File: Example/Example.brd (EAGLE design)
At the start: 86 x 54 mm, 25 parts, among them IC2 74LS02D, U1 CD4017

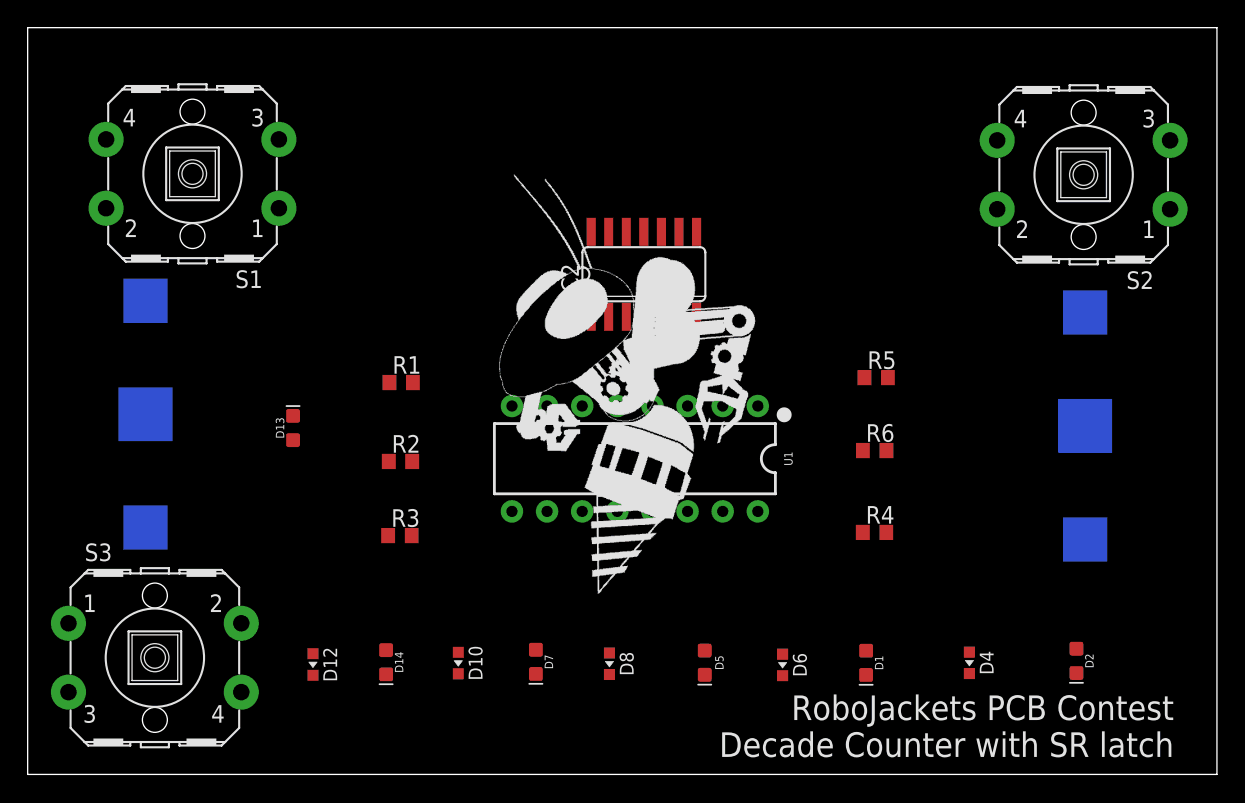
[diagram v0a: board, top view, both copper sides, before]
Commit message: made few routes except for gnd and vcc
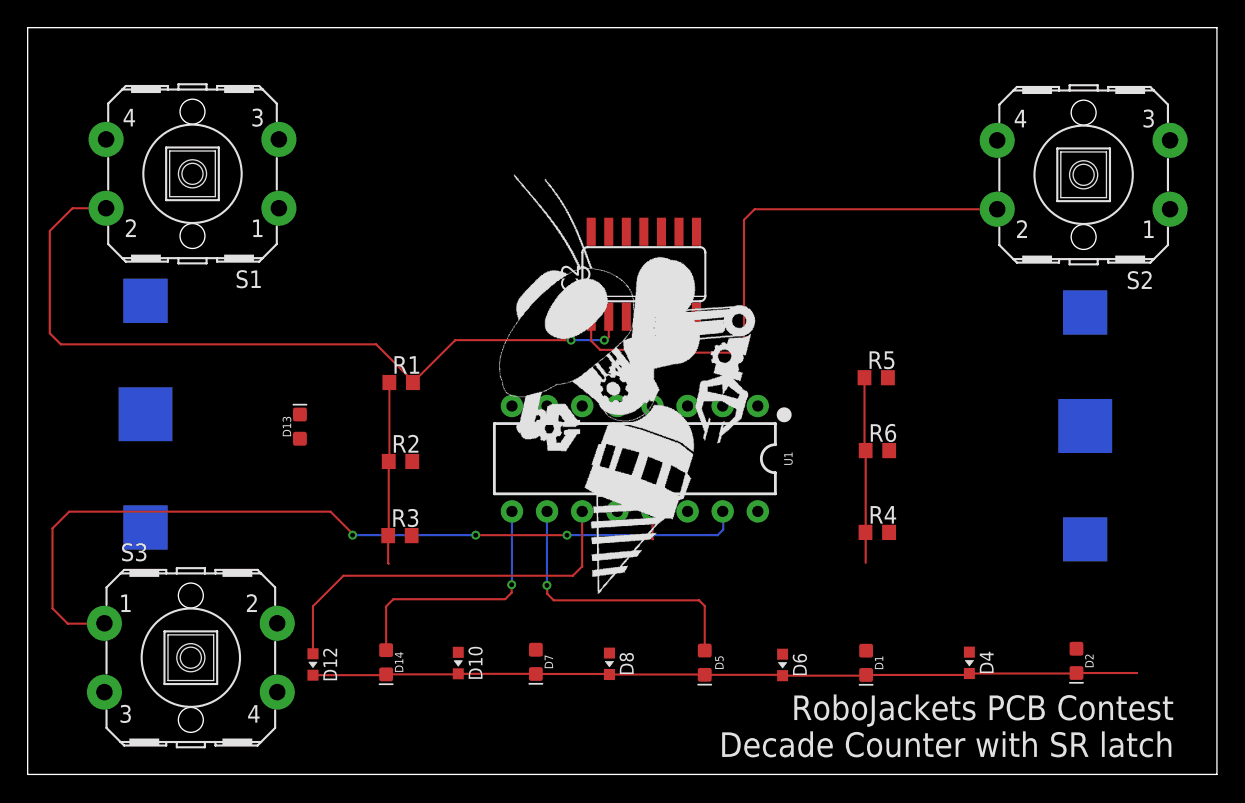
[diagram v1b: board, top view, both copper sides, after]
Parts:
- moved S3 2.60 mm to (11.8, 8.44)
- moved D13 0.51 mm to (19.7, 25.1)
- moved R6 0.20 mm to (61.5, 23.4)
- moved R4 0.20 mm to (61.4, 17.5)
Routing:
- net N$3: track 0.00 -> 61.3 mm, vias 0 -> 3
- net N$20: track 0.00 -> 59.7 mm
- net R: track 0.00 -> 56.9 mm, vias 0 -> 2
- net S: track 0.00 -> 34.6 mm
- net GND: track 0.00 -> 30.4 mm
- net N$19: track 0.00 -> 28.1 mm
- net N$14: track 0.00 -> 21.0 mm, vias 0 -> 1
- net N$18: track 0.00 -> 18.6 mm, vias 0 -> 1
- net Q: track 0.00 -> 9.06 mm

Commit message: add vcc and gnd planes and finished routing
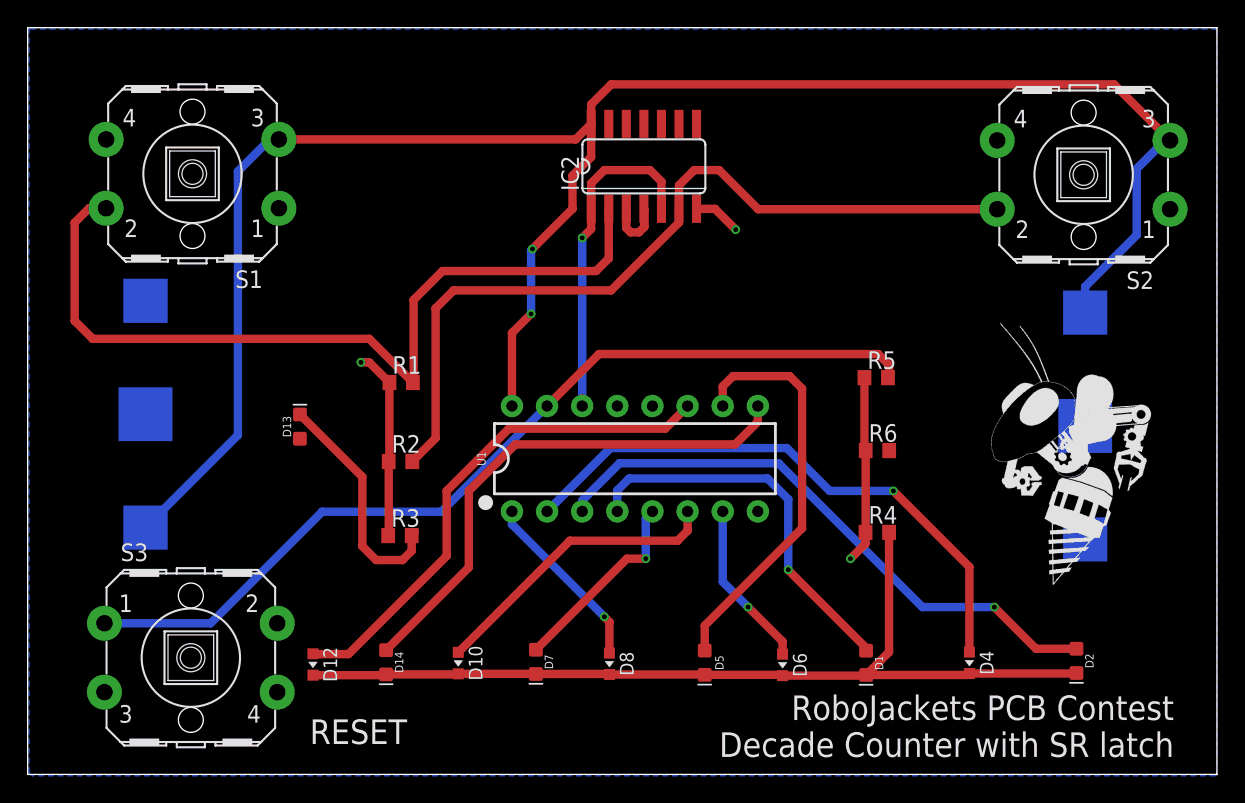
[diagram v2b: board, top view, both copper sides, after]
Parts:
- removed U$2: (no value), RoboJackets-Aesthetics:ROBOBUZZ_1.4X
- added U$4: (no value), RoboJackets-Aesthetics:ROBOBUZZ_1.0X
- moved IC2 7.80 mm to (44.6, 44.0)
- turned U1 to 0 degrees
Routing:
- net VCC: track 0.00 -> 139.0 mm, vias 0 -> 2
- net N$10: track 0.00 -> 43.2 mm, vias 0 -> 1
- net N$11: track 0.00 -> 42.2 mm, vias 0 -> 1
- net N$12: track 0.00 -> 28.1 mm, vias 0 -> 1
- net S: track 34.6 -> 59.3 mm
- net N$17: track 0.00 -> 21.7 mm
- net N$18: track 18.6 -> 38.1 mm, vias 1 -> 0
- net N$5: track 0.00 -> 17.1 mm
- net Q: track 9.06 -> 24.7 mm, vias 0 -> 1
- net N$16: track 0.00 -> 14.3 mm, vias 0 -> 1
- net N$15: track 0.00 -> 13.2 mm, vias 0 -> 1
- net N$13: track 0.00 -> 12.1 mm, vias 0 -> 1
- net N$19: track 28.1 -> 37.3 mm
- net N$14: track 21.0 -> 29.7 mm, vias 1 -> 0
- net N$20: track 59.7 -> 66.4 mm
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- added copper zone on layer 16, net GND
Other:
- board text added: "RESET"

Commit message: Added a layer for Vcc and GND, removed some routes
The GND routes and Vcc routes are connected to vias
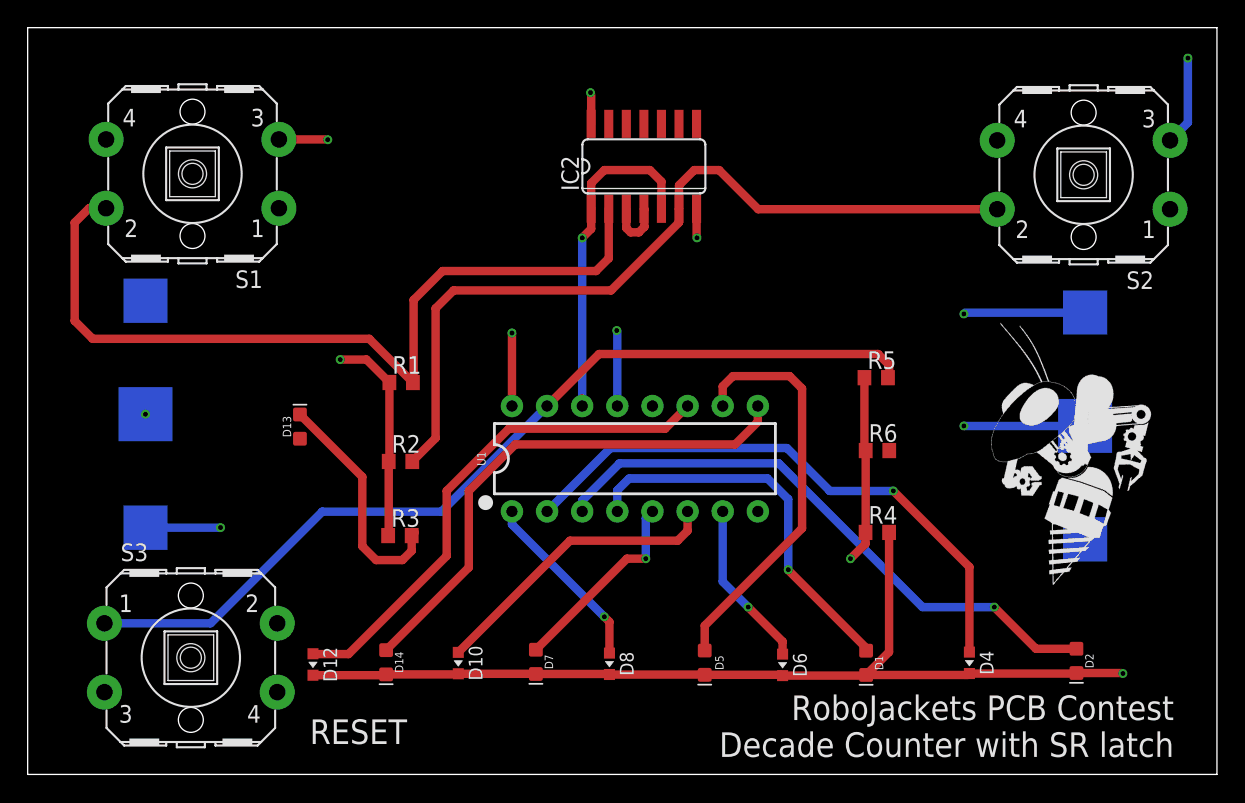
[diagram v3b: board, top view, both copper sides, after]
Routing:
- net VCC: track 139.0 -> 31.9 mm, vias 2 -> 6
- net GND: track 30.9 -> 45.6 mm, vias 3 -> 6
- net N$20: track 66.4 -> 69.8 mm, vias 0 -> 1
- removed copper zone on layer 16, net GND

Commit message: small changes
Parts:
- moved D13 1.28 mm to (20.7, 25.9)
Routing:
- net Q: track 24.7 -> 59.1 mm, vias 1 -> 3
- net VCC: track 31.9 -> 13.8 mm, vias 6 -> 3
- net GND: track 45.6 -> 29.0 mm, vias 6 -> 2
- net N$20: track 69.8 -> 66.4 mm, vias 1 -> 0
- net N$5: track 17.1 -> 18.7 mm
- net S: track 59.3 -> 60.6 mm
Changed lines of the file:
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@@
 <?xml version="1.0" encoding="utf-8"?>
 <!DOCTYPE eagle SYSTEM "eagle.dtd">
-<eagle version="9.5.2">
+<eagle version="9.5.1">
 <drawing>
 <settings>
-<setting alwaysvectorfont="no"/>
+<setting alwaysvectorfont="yes"/>
 <setting verticaltext="up"/>
 </settings>
@@
 <attribute name="VALUE" x="75.205" y="8.21" size="0.6096" layer="27" font="vector" ratio="20" rot="R270" align="top-center"/>
 </element>
-<element name="D13" library="RoboJackets-LEDs" package="LED-0603" value="GREEN" x="19.69" y="25.15" smashed="yes" rot="R90">
-<attribute name="NAME" x="19.055" y="25.15" size="0.6096" layer="25" font="vector" ratio="20" rot="R90" align="bottom-center"/>
-<attribute name="PROD_ID" value="DIO-00821" x="19.69" y="25.15" size="1.778" layer="27" rot="R90" display="off"/>
-<attribute name="VALUE" x="20.325" y="25.15" size="0.6096" layer="27" font="vector" ratio="20" rot="R90" align="top-center"/>
+<element name="D13" library="RoboJackets-LEDs" package="LED-0603" value="GREEN" x="20.69" y="25.95" smashed="yes" rot="R90">
+<attribute name="NAME" x="20.055" y="25.95" size="0.6096" layer="25" font="vector" ratio="20" rot="R90" align="bottom-center"/>
+<attribute name="PROD_ID" value="DIO-00821" x="20.69" y="25.95" size="1.778" layer="27" rot="R90" display="off"/>
+<attribute name="VALUE" x="21.325" y="25.95" size="0.6096" layer="27" font="vector" ratio="20" rot="R90" align="top-center"/>
 </element>
 <element name="D14" library="RoboJackets-LEDs" package="LED-0603" value="BLUE" x="25.92" y="8.11" smashed="yes" rot="R270">
@@
 <signals>
 <signal name="GND">
-<contactref element="IC2" pad="7"/>
 <contactref element="R1" pad="1"/>
 <contactref element="R2" pad="1"/>
@@
 <wire x1="26.11" y1="22.63" x2="26.11" y2="17.31" width="0.6096" layer="1"/>
 <wire x1="26.11" y1="17.31" x2="26.07" y2="17.27" width="0.1524" layer="1"/>
-<wire x1="48.4" y1="40.8666" x2="48.37" y2="40.8966" width="0.1524" layer="1"/>
 <wire x1="60.51" y1="28.69" x2="60.51" y2="23.51" width="0.6096" layer="1"/>
 <wire x1="60.51" y1="23.51" x2="60.6" y2="23.42" width="0.1524" layer="1"/>
@@
 <wire x1="24.5" y1="30" x2="22.6" y2="30" width="0.6096" layer="1"/>
 <via x="22.6" y="30" extent="1-16" drill="0.35"/>
-<via x="8.52" y="26.05" extent="1-16" drill="0.35"/>
-<wire x1="48.2" y1="40.7266" x2="48.37" y2="40.8966" width="0.1524" layer="1"/>
-<wire x1="48.37" y1="40.8966" x2="48.37" y2="38.83" width="0.6096" layer="1"/>
-<wire x1="48.37" y1="38.83" x2="48.4" y2="38.8" width="0.1524" layer="1"/>
-<via x="48.4" y="38.8" extent="1-16" drill="0.35"/>
-<wire x1="76.47" y1="25.2" x2="67.7" y2="25.2" width="0.6096" layer="16"/>
-<via x="67.7" y="25.2" extent="1-16" drill="0.35"/>
-<wire x1="42.64" y1="26.64" x2="42.64" y2="32.06" width="0.6096" layer="16"/>
-<wire x1="42.64" y1="32.06" x2="42.6" y2="32.1" width="0.1524" layer="16"/>
-<via x="42.6" y="32.1" extent="1-16" drill="0.35"/>
-<wire x1="60.6" y1="23.42" x2="67.7" y2="25.2" width="0" layer="19" extent="1-1"/>
-<wire x1="48.4" y1="38.8" x2="60.51" y2="28.69" width="0" layer="19" extent="1-1"/>
-<wire x1="42.6" y1="32.1" x2="48.4" y2="38.8" width="0" layer="19" extent="1-1"/>
+<contactref element="IC2" pad="7"/>
+<wire x1="60.6" y1="23.42" x2="76.47" y2="25.2" width="0" layer="19" extent="1-16"/>
+<wire x1="48.37" y1="40.8966" x2="60.51" y2="28.69" width="0" layer="19" extent="1-1"/>
+<wire x1="42.64" y1="26.64" x2="48.37" y2="40.8966" width="0" layer="19" extent="1-1"/>
 <wire x1="26.16" y1="28.34" x2="42.64" y2="26.64" width="0" layer="19" extent="1-1"/>
 <wire x1="8.52" y1="26.05" x2="22.6" y2="30" width="0" layer="19" extent="16-16"/>
 </signal>
 <signal name="VCC">
-<contactref element="IC2" pad="14"/>
 <contactref element="S1" pad="3"/>
 <contactref element="S2" pad="3"/>
@@
 <contactref element="U$3" pad="+$1"/>
 <contactref element="U1" pad="16"/>
-<wire x1="35.02" y1="26.64" x2="35.02" y2="31.92" width="0.6096" layer="1"/>
-<wire x1="8.52" y1="17.85" x2="13.85" y2="17.85" width="0.6096" layer="16"/>
-<wire x1="13.85" y1="17.85" x2="13.9" y2="17.8" width="0.1524" layer="16"/>
-<wire x1="13.9" y1="17.8" x2="13.95" y2="17.85" width="0.1524" layer="16"/>
-<via x="13.95" y="17.85" extent="1-16" drill="0.35"/>
+<wire x1="8.52" y1="17.85" x2="12.35" y2="17.85" width="0.6096" layer="16"/>
+<wire x1="13.65" y1="16.55" x2="12.35" y2="17.85" width="0.6096" layer="16"/>
+<via x="13.65" y="16.55" extent="1-16" drill="0.35"/>
+<wire x1="76.47" y1="33.4" x2="73.3" y2="33.4" width="0.6096" layer="16"/>
+<wire x1="73.3" y1="33.4" x2="72.2" y2="32.3" width="0.6096" layer="16"/>
+<via x="72.2" y="32.3" extent="1-16" drill="0.35"/>
+<contactref element="IC2" pad="14"/>
 <wire x1="40.75" y1="47.0434" x2="40.75" y2="49.15" width="0.6096" layer="1"/>
-<wire x1="40.75" y1="49.15" x2="40.8" y2="49.2" width="0.1524" layer="1"/>
-<wire x1="40.8" y1="49.2" x2="40.7" y2="49.3" width="0.1524" layer="1"/>
-<via x="40.7" y="49.3" extent="1-16" drill="0.35"/>
-<wire x1="82.6084" y1="45.8492" x2="83.9" y2="47.1408" width="0.6096" layer="16"/>
-<wire x1="83.9" y1="47.1408" x2="83.9" y2="51.8" width="0.6096" layer="16"/>
-<via x="83.9" y="51.8" extent="1-16" drill="0.35"/>
-<wire x1="76.47" y1="33.4" x2="67.8" y2="33.4" width="0.6096" layer="16"/>
-<wire x1="67.8" y1="33.4" x2="67.7" y2="33.3" width="0.1524" layer="16"/>
-<via x="67.7" y="33.3" extent="1-16" drill="0.35"/>
-<via x="35.02" y="31.92" extent="1-16" drill="0.35"/>
-<wire x1="18.1684" y1="45.9192" x2="21.5808" y2="45.9192" width="0.6096" layer="1"/>
-<wire x1="21.5808" y1="45.9192" x2="21.6" y2="45.9" width="0.1524" layer="1"/>
-<wire x1="21.6" y1="45.9" x2="21.7" y2="45.9" width="0.1524" layer="1"/>
-<via x="21.7" y="45.9" extent="1-16" drill="0.35"/>
+<wire x1="40.75" y1="49.15" x2="39.8" y2="50.1" width="0.6096" layer="1"/>
+<via x="39.8" y="50.1" extent="1-16" drill="0.35"/>
 <wire x1="76.47" y1="33.4" x2="82.6084" y2="45.8492" width="0" layer="19" extent="16-16"/>
-<wire x1="40.75" y1="47.0434" x2="67.7" y2="33.3" width="0" layer="19" extent="1-1"/>
-<wire x1="35.02" y1="31.92" x2="40.75" y2="47.0434" width="0" layer="19" extent="1-1"/>
-<wire x1="21.7" y1="45.9" x2="40.75" y2="47.0434" width="0" layer="19" extent="1-1"/>
-<wire x1="13.95" y1="17.85" x2="35.02" y2="26.64" width="0" layer="19" extent="1-1"/>
+<wire x1="40.75" y1="47.0434" x2="72.2" y2="32.3" width="0" layer="19" extent="1-1"/>
+<wire x1="35.02" y1="26.64" x2="40.75" y2="47.0434" width="0" layer="19" extent="1-1"/>
+<wire x1="18.1684" y1="45.9192" x2="39.8" y2="50.1" width="0" layer="19" extent="1-1"/>
+<wire x1="13.65" y1="16.55" x2="35.02" y2="26.64" width="0" layer="19" extent="1-1"/>
 </signal>
 <signal name="QNOT">
@@
 <via x="40.1" y="38.8" extent="1-16" drill="0.35"/>
 <wire x1="40.1" y1="38.8" x2="40.1" y2="26.64" width="0.6096" layer="16"/>
-<wire x1="40.1" y1="26.64" x2="62.3" y2="23.42" width="0" layer="19" extent="1-1"/>
+<wire x1="62.3" y1="23.42" x2="64.4" y2="25.52" width="0.6096" layer="1"/>
+<wire x1="64.4" y1="25.52" x2="64.4" y2="30.1" width="0.6096" layer="1"/>
+<wire x1="64.4" y1="30.1" x2="62.6" y2="31.9" width="0.6096" layer="1"/>
+<wire x1="62.6" y1="31.9" x2="48.5" y2="31.9" width="0.6096" layer="1"/>
+<wire x1="45.9" y1="34.4" x2="46" y2="34.4" width="0.6096" layer="1"/>
+<wire x1="48.5" y1="31.9" x2="46" y2="34.4" width="0.6096" layer="1"/>
+<via x="45.9" y="34.4" extent="1-16" drill="0.35"/>
+<wire x1="45.9" y1="34.4" x2="45.9" y2="38.4" width="0.6096" layer="16"/>
+<wire x1="45.9" y1="38.4" x2="45.8" y2="38.5" width="0.6096" layer="16"/>
+<via x="45.8" y="38.5" extent="1-16" drill="0.35"/>
+<wire x1="45.8" y1="38.5" x2="45.8" y2="40.8666" width="0.6096" layer="1"/>
+<wire x1="45.8" y1="40.8666" x2="45.83" y2="40.8966" width="0.6096" layer="1"/>
 </signal>
 <signal name="S">
@@
 <wire x1="48.2" y1="43.7" x2="47.1" y2="42.6" width="0.6096" layer="1"/>
 <wire x1="47.1" y1="40.8966" x2="47.092" y2="40.8886" width="0.6096" layer="1"/>
-<wire x1="47.092" y1="40.8886" x2="47.092" y2="39.90174375" width="0.6096" layer="1"/>
-<wire x1="47.092" y1="39.90174375" x2="42.19025625" y2="35" width="0.6096" layer="1"/>
-<wire x1="42.19025625" y1="35" x2="30.8" y2="35" width="0.6096" layer="1"/>
+<wire x1="47.092" y1="40.8886" x2="47.092" y2="37.60174375" width="0.6096" layer="1"/>
+<wire x1="47.092" y1="37.60174375" x2="44.49025625" y2="35" width="0.6096" layer="1"/>
+<wire x1="44.49025625" y1="35" x2="30.8" y2="35" width="0.6096" layer="1"/>
 <wire x1="30.8" y1="35" x2="29.5" y2="33.7" width="0.6096" layer="1"/>
 <wire x1="29.5" y1="24.32" x2="27.81" y2="22.63" width="0.6096" layer="1"/>
@@
 <contactref element="D13" pad="C"/>
 <wire x1="28" y1="17.5" x2="27.77" y2="17.27" width="0.6096" layer="1"/>
-<wire x1="19.69" y1="26.027" x2="24.2" y2="21.517" width="0.6096" layer="1"/>
-<wire x1="24.2" y1="21.517" x2="24.2" y2="16.5" width="0.6096" layer="1"/>
 <wire x1="24.2" y1="16.5" x2="25.2" y2="15.5" width="0.6096" layer="1"/>
 <wire x1="25.2" y1="15.5" x2="27.1" y2="15.5" width="0.6096" layer="1"/>
 <wire x1="27.77" y1="16.17" x2="27.77" y2="17.27" width="0.6096" layer="1"/>
 <wire x1="27.1" y1="15.5" x2="27.77" y2="16.17" width="0.6096" layer="1"/>
+<wire x1="20.69" y1="26.827" x2="22.773" y2="26.827" width="0.6096" layer="1"/>
+<wire x1="22.773" y1="26.827" x2="24.2" y2="25.4" width="0.6096" layer="1"/>
+<wire x1="24.2" y1="25.4" x2="24.2" y2="16.5" width="0.6096" layer="1"/>
 </signal>
 <signal name="N$10">
@@
 <wire x1="62.29" y1="17.5" x2="62.29" y2="8.853" width="0.6096" layer="1"/>
 <wire x1="62.29" y1="8.853" x2="60.63" y2="7.193" width="0.6096" layer="1"/>
-<wire x1="75.84" y1="7.333" x2="79.067" y2="7.333" width="0.6096" layer="1"/>
-<wire x1="79.067" y1="7.333" x2="79.1" y2="7.3" width="0.1524" layer="1"/>
-<wire x1="79.1" y1="7.3" x2="79.2" y2="7.3" width="0.1524" layer="1"/>
-<via x="79.2" y="7.3" extent="1-16" drill="0.35"/>
 </signal>
 <signal name="N$1">
